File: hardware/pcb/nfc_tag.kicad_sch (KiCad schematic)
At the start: 15 parts, among them J1 debug/prog, U1 ATtiny402, U2 ST25DV04K

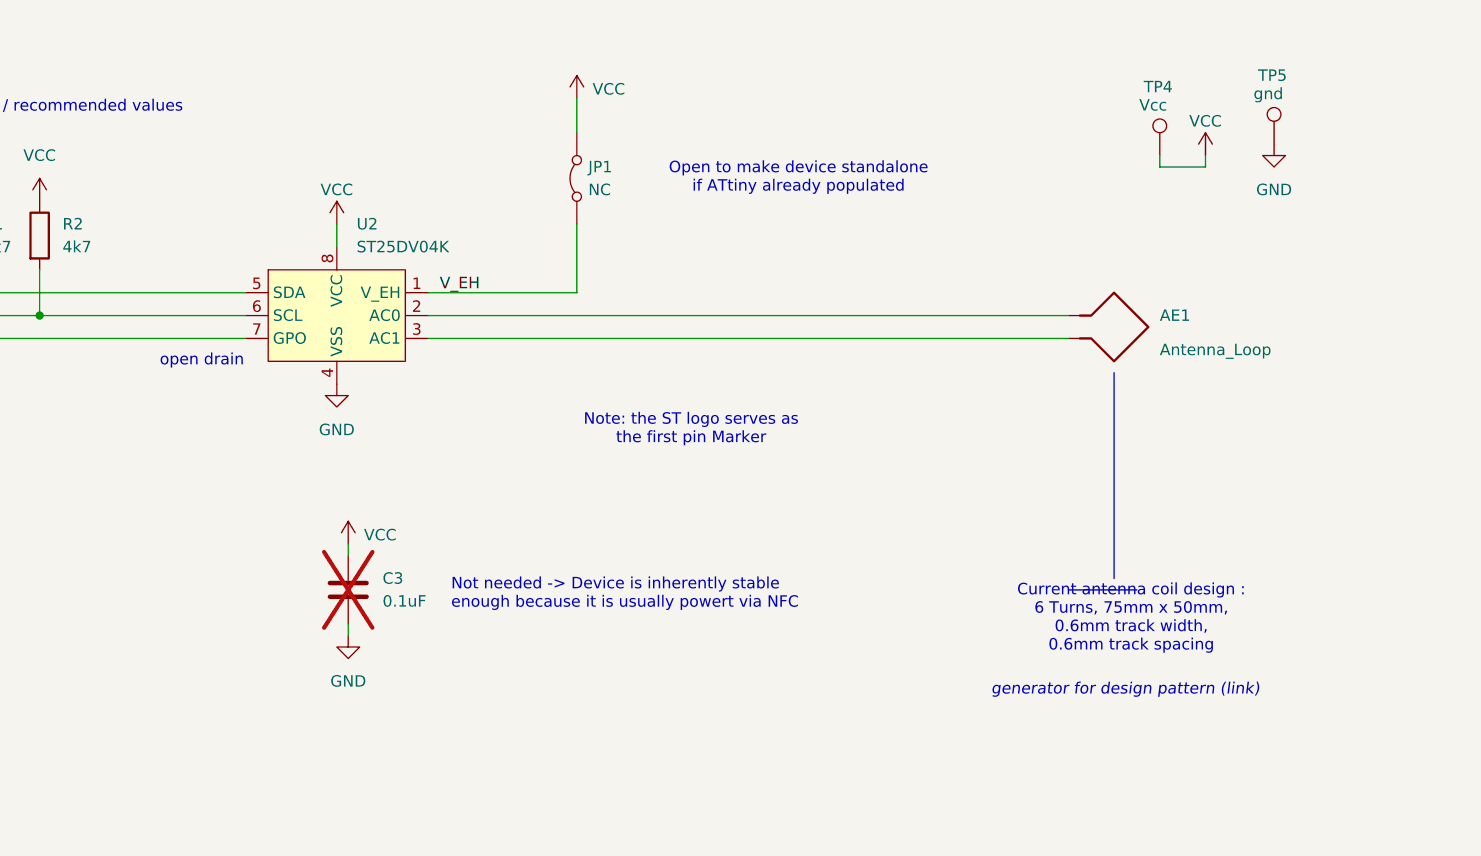
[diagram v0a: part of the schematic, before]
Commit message: improved schematic clarity and fixed sight mistake in csv
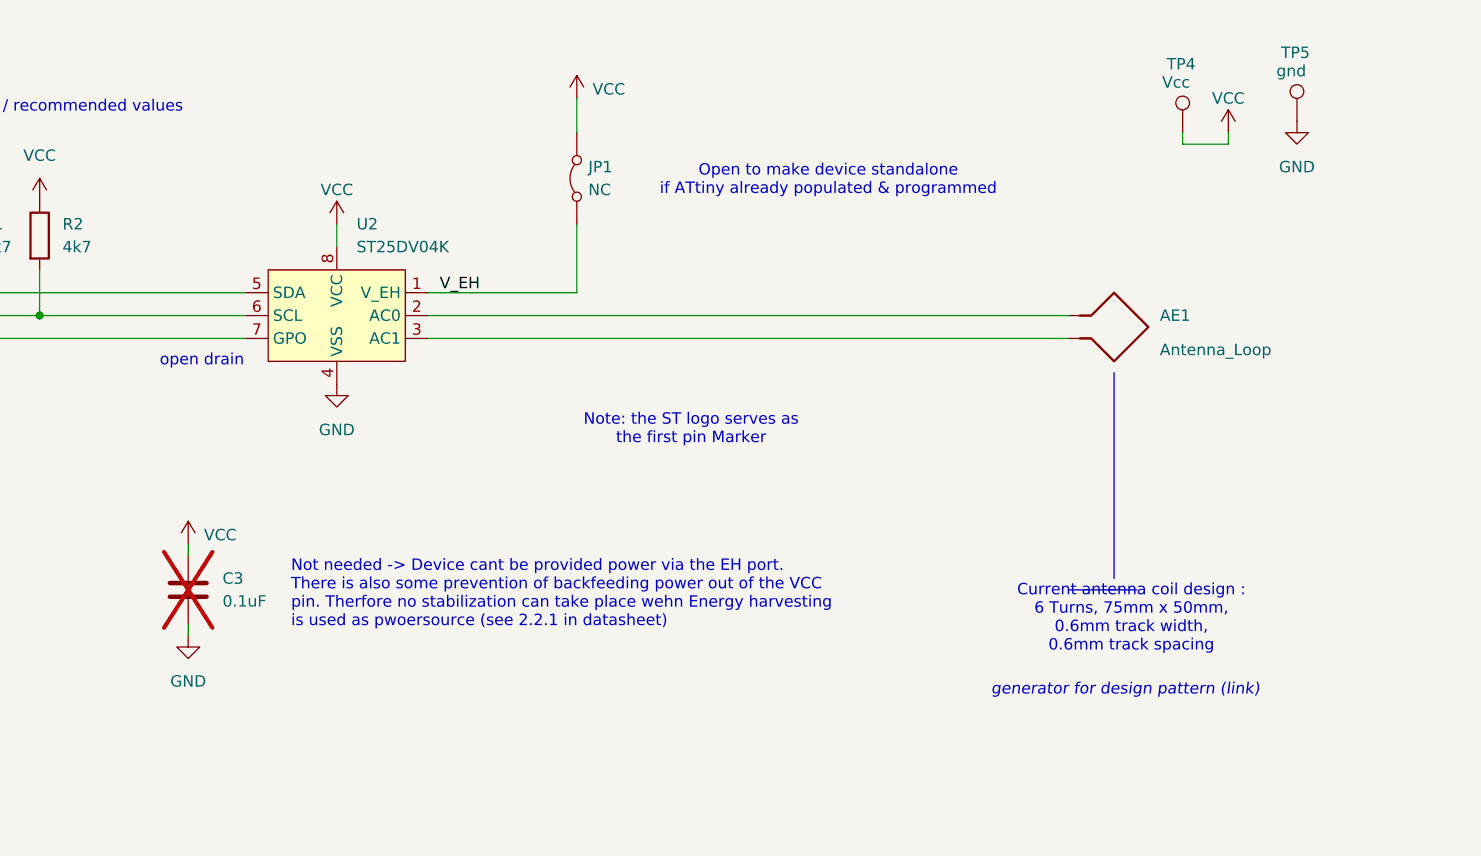
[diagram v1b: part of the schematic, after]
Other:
- note added: "Not needed -> Device cant be provided power via the EH port. There is also some prevention of backfeeding power out of the VCC pin. Therfore no stabilization can take place wehn Energy harvesting is used as pwoersource (see 2.2.1 in datasheet)"
- note added: "Open to make device standalone if ATtiny already populated & programmed"
- note removed: "Not needed -> Device is inherently stable enough because it is usually powert via NFC"
- note removed: "Open to make device standalone if ATtiny already populated"
- moved on the sheet: C3, TP4, TP5
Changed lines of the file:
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@@
 	(wire
 		(pts
-			(xy 248.92 45.72) (xy 254 45.72)
+			(xy 251.46 43.18) (xy 256.54 43.18)
 		)
 		(stroke
@@
 	(wire
 		(pts
-			(xy 248.92 45.72) (xy 248.92 44.45)
+			(xy 251.46 43.18) (xy 251.46 41.91)
 		)
 		(stroke
@@
 	(wire
 		(pts
-			(xy 254 45.72) (xy 254 44.45)
+			(xy 256.54 43.18) (xy 256.54 41.91)
 		)
 		(stroke
@@
 	(wire
 		(pts
-			(xy 158.75 96.52) (xy 158.75 97.79)
+			(xy 140.97 96.52) (xy 140.97 97.79)
 		)
 		(stroke
@@
 	(wire
 		(pts
-			(xy 158.75 88.9) (xy 158.75 87.63)
+			(xy 140.97 88.9) (xy 140.97 87.63)
 		)
 		(stroke
@@
 		)
 	)
-	(text "Not needed -> Device is inherently stable \nenough because it is usually powert via NFC"
+	(text "Not needed -> Device cant be provided power via the EH port. \nThere is also some prevention of backfeeding power out of the VCC\npin. Therfore no stabilization can take place wehn Energy harvesting \nis used as pwoersource (see 2.2.1 in datasheet)"
 		(exclude_from_sim no)
-		(at 170.18 93.218 0)
+		(at 152.4 93.218 0)
 		(effects
 			(font
@@
 		)
 	)
-	(text "Open to make device standalone \nif ATtiny already populated\n\n"
+	(text "Open to make device standalone \nif ATtiny already populated & programmed\n"
 		(exclude_from_sim no)
-		(at 208.788 48.006 0)
+		(at 212.09 47.244 0)
 		(effects
 			(font
@@
 	(symbol
 		(lib_id "Device:C")
-		(at 158.75 92.71 0)
+		(at 140.97 92.71 0)
 		(unit 1)
 		(exclude_from_sim no)
@@
 		(fields_autoplaced yes)
 		(property "Reference" "C3"
-			(at 162.56 91.4399 0)
+			(at 144.78 91.4399 0)
 			(effects
 				(font
@@
 		)
 		(property "Value" "0.1uF"
-			(at 162.56 93.9799 0)
+			(at 144.78 93.9799 0)
 			(effects
 				(font
@@
 		)
 		(property "Footprint" "Capacitor_SMD:C_0603_1608Metric_Pad1.08x0.95mm_HandSolder"
-			(at 159.7152 96.52 0)
+			(at 141.9352 96.52 0)
 			(effects
 				(font
@@
 		)
 		(property "Datasheet" "~"
-			(at 158.75 92.71 0)
+			(at 140.97 92.71 0)
 			(effects
 				(font
@@
 		)
 		(property "Description" "Unpolarized capacitor"
-			(at 158.75 92.71 0)
+			(at 140.97 92.71 0)
 			(effects
 				(font
@@
 		)
 		(property "Digikeynumber" "1276-1000-1-ND"
-			(at 158.75 92.71 0)
+			(at 140.97 92.71 0)
 			(effects
 				(font
@@
 	(symbol
 		(lib_id "Connector:TestPoint")
-		(at 248.92 44.45 0)
+		(at 251.46 41.91 0)
 		(unit 1)
 		(exclude_from_sim no)
@@
 		(dnp no)
 		(property "Reference" "TP4"
-			(at 247.142 36.83 0)
+			(at 249.682 34.29 0)
 			(effects
 				(font
@@
 		)
 		(property "Value" "Vcc"
-			(at 246.634 38.862 0)
+			(at 249.174 36.322 0)
 			(effects
 				(font
@@
 		)
 		(property "Footprint" "TestPoint:TestPoint_Pad_D1.5mm"
-			(at 254 44.45 0)
+			(at 256.54 41.91 0)
 			(effects
 				(font
@@
 		)
 		(property "Datasheet" "~"
-			(at 254 44.45 0)
+			(at 256.54 41.91 0)
 			(effects
 				(font
@@
 		)
 		(property "Description" "test point"
-			(at 248.92 44.45 0)
+			(at 251.46 41.91 0)
 			(effects
 				(font
@@
 		)
 		(property "Digikeynumber" "~"
-			(at 248.92 44.45 0)
+			(at 251.46 41.91 0)
 			(effects
 				(font
@@
 	(symbol
 		(lib_id "power:GND")
-		(at 261.62 43.18 0)
+		(at 264.16 40.64 0)
 		(unit 1)
 		(exclude_from_sim no)
@@
 		(fields_autoplaced yes)
 		(property "Reference" "#PWR012"
-			(at 261.62 49.53 0)
+			(at 264.16 46.99 0)
 			(effects
 				(font
@@
 		)
 		(property "Value" "GND"
-			(at 261.62 48.26 0)
+			(at 264.16 45.72 0)
 			(effects
 				(font
@@
 		)
 		(property "Footprint" ""
-			(at 261.62 43.18 0)
+			(at 264.16 40.64 0)
 			(effects
 				(font
@@
 		)
 		(property "Datasheet" ""
-			(at 261.62 43.18 0)
+			(at 264.16 40.64 0)
 			(effects
 				(font
@@
 		)
 		(property "Description" "Power symbol creates a global label with name \"GND\" , ground"
-			(at 261.62 43.18 0)
+			(at 264.16 40.64 0)
 			(effects
 				(font
@@
 	(symbol
 		(lib_id "power:VCC")
-		(at 158.75 87.63 0)
+		(at 140.97 87.63 0)
 		(unit 1)
 		(exclude_from_sim no)
@@
 		(dnp no)
 		(property "Reference" "#PWR013"
-			(at 158.75 91.44 0)
+			(at 140.97 91.44 0)
 			(effects
 				(font
@@
 		)
 		(property "Value" "VCC"
-			(at 162.306 86.614 0)
+			(at 144.526 86.614 0)
 			(effects
 				(font
@@
 		)
 		(property "Footprint" ""
-			(at 158.75 87.63 0)
+			(at 140.97 87.63 0)
 			(effects
 				(font
@@
 		)
 		(property "Datasheet" ""
-			(at 158.75 87.63 0)
+			(at 140.97 87.63 0)
 			(effects
 				(font
@@
 		)
 		(property "Description" "Power symbol creates a global label with name \"VCC\""
-			(at 158.75 87.63 0)
+			(at 140.97 87.63 0)
 			(effects
 				(font
@@
 	(symbol
 		(lib_id "power:VCC")
-		(at 254 44.45 0)
+		(at 256.54 41.91 0)
 		(unit 1)
 		(exclude_from_sim no)
@@
 		(dnp no)
 		(property "Reference" "#PWR011"
-			(at 254 48.26 0)
+			(at 256.54 45.72 0)
 			(effects
 				(font
@@
 		)
 		(property "Value" "VCC"
-			(at 254 40.64 0)
+			(at 256.54 38.1 0)
 			(effects
 				(font
@@
 		)
 		(property "Footprint" ""
-			(at 254 44.45 0)
+			(at 256.54 41.91 0)
 			(effects
 				(font
@@
 		)
 		(property "Datasheet" ""
-			(at 254 44.45 0)
+			(at 256.54 41.91 0)
 			(effects
 				(font
@@
 		)
 		(property "Description" "Power symbol creates a global label with name \"VCC\""
-			(at 254 44.45 0)
+			(at 256.54 41.91 0)
 			(effects
 				(font
@@
 	(symbol
 		(lib_id "power:GND")
-		(at 158.75 97.79 0)
+		(at 140.97 97.79 0)
 		(unit 1)
 		(exclude_from_sim no)
@@
 		(fields_autoplaced yes)
 		(property "Reference" "#PWR014"
-			(at 158.75 104.14 0)
+			(at 140.97 104.14 0)
 			(effects
 				(font
@@
 		)
 		(property "Value" "GND"
-			(at 158.75 102.87 0)
+			(at 140.97 102.87 0)
 			(effects
 				(font
@@
 		)
 		(property "Footprint" ""
-			(at 158.75 97.79 0)
+			(at 140.97 97.79 0)
 			(effects
 				(font
@@
 		)
 		(property "Datasheet" ""
-			(at 158.75 97.79 0)
+			(at 140.97 97.79 0)
 			(effects
 				(font
@@
 		)
 		(property "Description" "Power symbol creates a global label with name \"GND\" , ground"
-			(at 158.75 97.79 0)
+			(at 140.97 97.79 0)
 			(effects
 				(font
@@
 	(symbol
 		(lib_id "Connector:TestPoint")
-		(at 261.62 43.18 0)
+		(at 264.16 40.64 0)
 		(unit 1)
 		(exclude_from_sim no)
@@
 		(dnp no)
 		(property "Reference" "TP5"
-			(at 259.842 35.56 0)
+			(at 262.382 33.02 0)
 			(effects
 				(font
@@
 		)
 		(property "Value" "gnd"
-			(at 259.334 37.592 0)
+			(at 261.874 35.052 0)
 			(effects
 				(font
@@
 		)
 		(property "Footprint" "TestPoint:TestPoint_Pad_D1.5mm"
-			(at 266.7 43.18 0)
+			(at 269.24 40.64 0)
 			(effects
 				(font
@@
 		)
 		(property "Datasheet" "~"
-			(at 266.7 43.18 0)
+			(at 269.24 40.64 0)
 			(effects
 				(font
@@
 		)
 		(property "Description" "test point"
-			(at 261.62 43.18 0)
+			(at 264.16 40.64 0)
 			(effects
 				(font
@@
 		)
 		(property "Digikeynumber" "~"
-			(at 261.62 43.18 0)
+			(at 264.16 40.64 0)
 			(effects
 				(font
